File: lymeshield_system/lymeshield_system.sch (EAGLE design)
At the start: 67 parts, among them IC1 MCP79410-I_SN, J1 TSW-106-07-G-S, J2 M04B, J3 TSW-103-07-G-D-LL, J4 1844210, U1 ATMEGA1608-MU, U10 STSPIN240, U2 MX25V1635FM1I, U3 OPA2349EA, U4 DRV5057A2QDBZ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

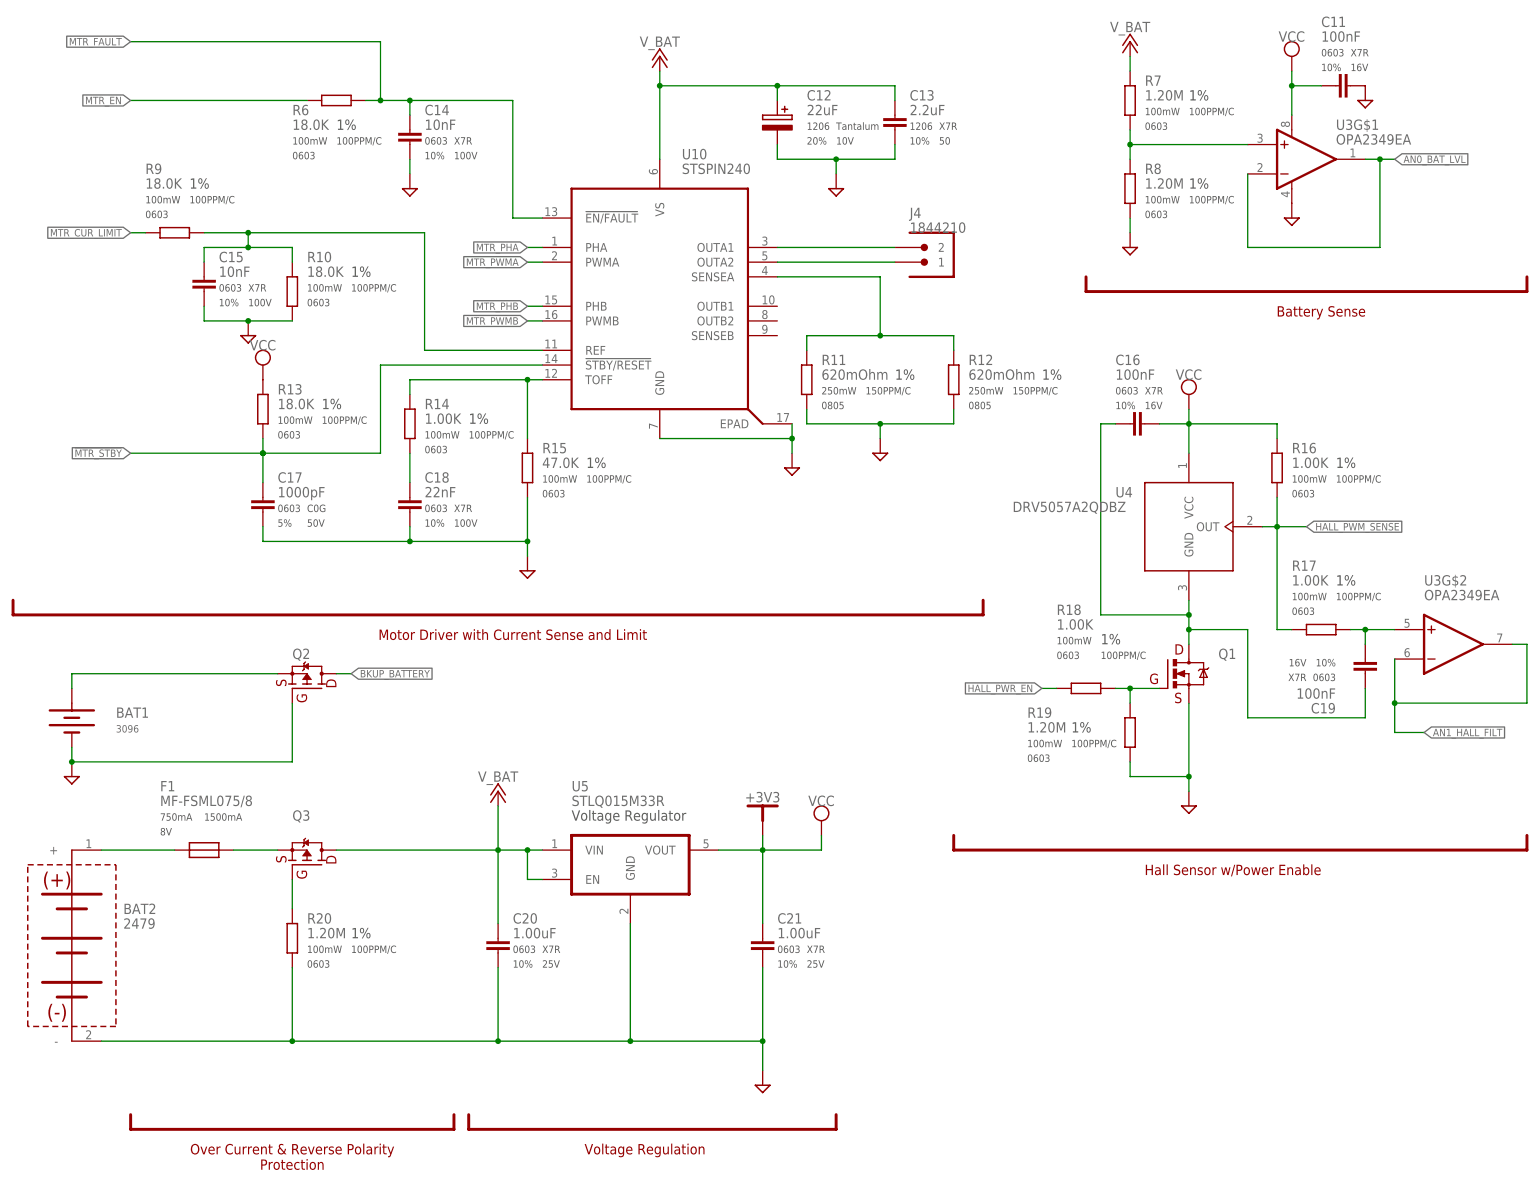
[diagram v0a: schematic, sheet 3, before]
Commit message: refactor: fixed ignored files and added tables
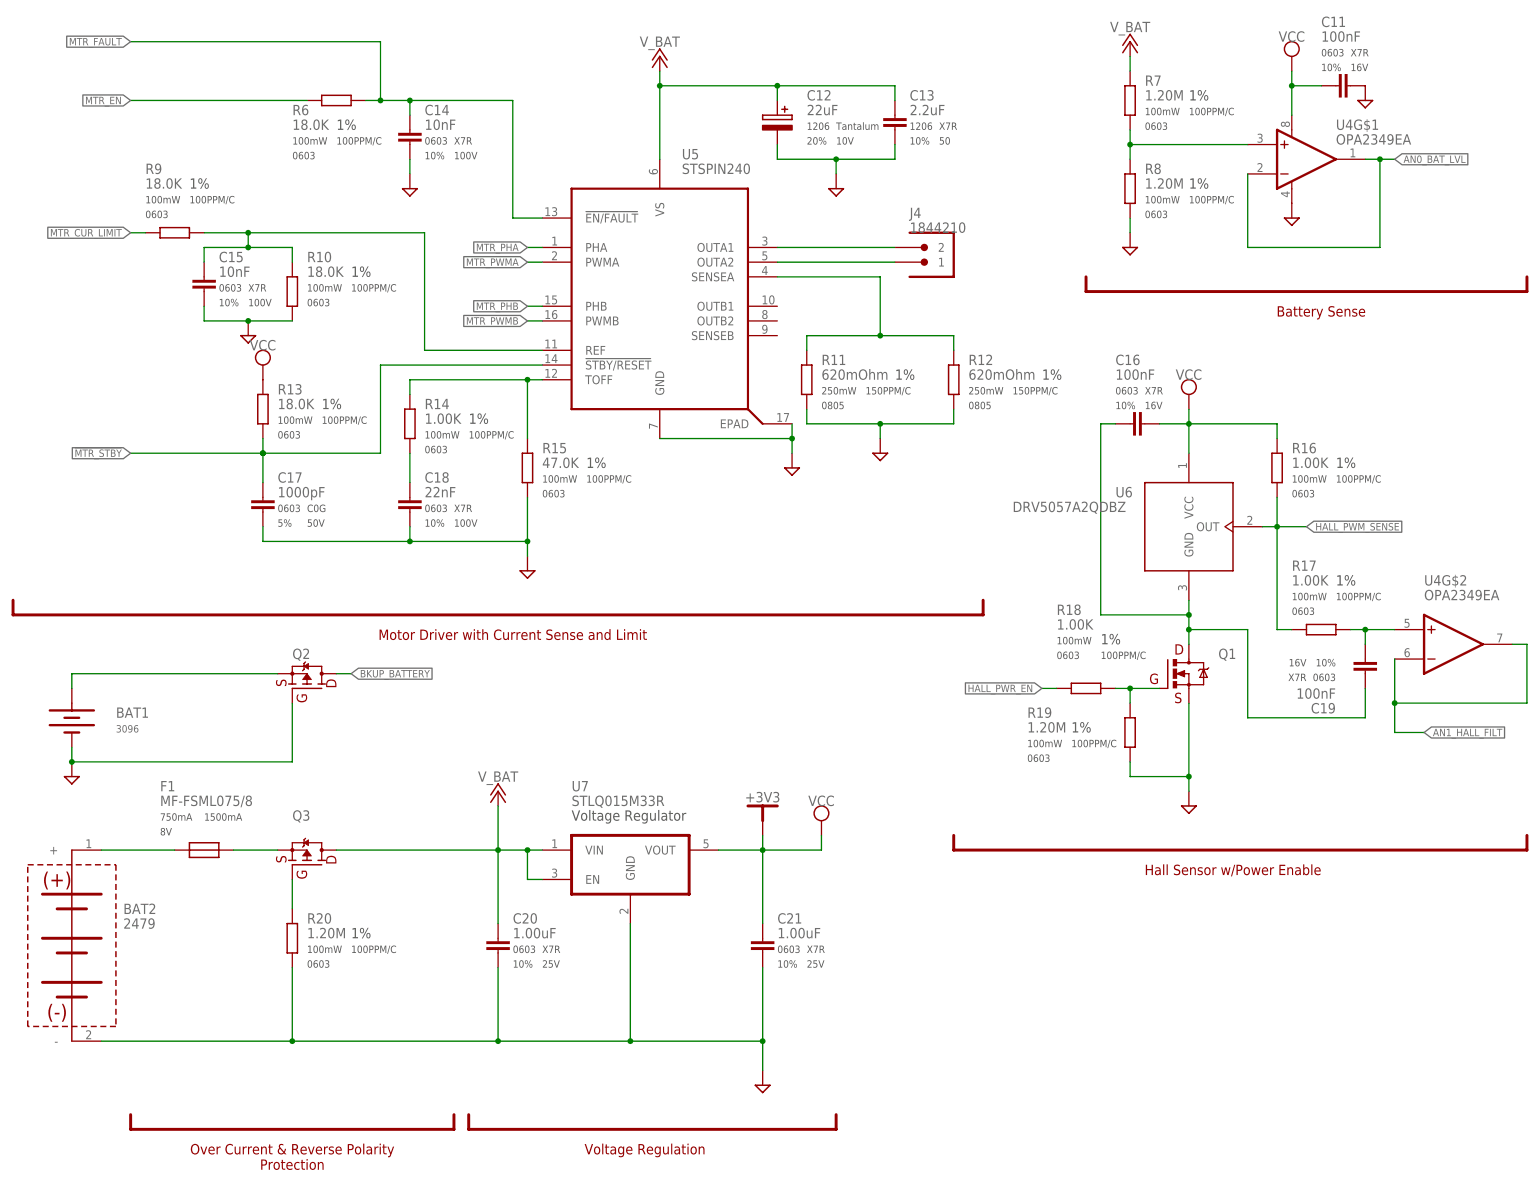
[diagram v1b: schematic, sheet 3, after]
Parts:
- removed IC1: MCP79410-I_SN, HatchPoint-MicrochipTechnology:MCP79410-I_SN
- removed U10: STSPIN240, HatchPoint-TI:STSPIN240
- added U6: DRV5057A2QDBZ, HatchPoint-TI:DRV5057A2QDBZ
- added U7: STLQ015M33R, HatchPoint-ST:STLQ015M33R
- U1: value ATMEGA1608-MU -> MCP79410-I_SN; device HatchPoint-MicrochipTechnology:ATMEGA1608-MU -> HatchPoint-MicrochipTechnology:MCP79410-I_SN
- U2: value MX25V1635FM1I -> ATMEGA1608-MU; device HatchPoint-Macronix:MX25V1635FM1I -> HatchPoint-MicrochipTechnology:ATMEGA1608-MU
- U3: value OPA2349EA -> MX25V1635FM1I; device HatchPoint-OPAMPs:OPA2349EA -> HatchPoint-Macronix:MX25V1635FM1I
- U4: value DRV5057A2QDBZ -> OPA2349EA; device HatchPoint-TI:DRV5057A2QDBZ -> HatchPoint-OPAMPs:OPA2349EA
- U5: value STLQ015M33R -> STSPIN240; device HatchPoint-ST:STLQ015M33R -> HatchPoint-TI:STSPIN240
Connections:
- net !CS_FLASH: now also U2.PA3, U3.!CS; no longer U1.PA3, U2.!CS
- net !GRN_LED_EN: now also U2.PD1; no longer U1.PD1
- net !MTR_FAULT: now also U2.PD5; no longer U1.PD5
- net !MTR_STBY: now also U2.PD7, U5.!STBY/RESET; no longer U1.PD7, U10.!STBY/RESET
- net !RED_LED_EN: now also U2.PD0; no longer U1.PD0
- net !RST: now also U2.PF6(!RST); no longer U1.PF6(!RST)
- net AN0_BAT_LVL: now also U2.PD3, U4G$1.-IN, U4G$1.OUT; no longer U1.PD3, U3G$1.-IN, U3G$1.OUT
- net AN1_HALL_FILT: now also U2.PD4, U4G$2.-IN, U4G$2.OUT; no longer U1.PD4, U3G$2.-IN, U3G$2.OUT
- net AVDD: now also U2.AVDD; no longer U1.AVDD
- net BKUP_BATTERY: now also U1.VBAT; no longer IC1.VBAT
- net DGND: now also U1.VSS, U2.EP, U2.GND@1, U2.GND@2, U3.GND, U4G$1.V-, U5.EPAD, U7.GND; no longer IC1.VSS, U1.EP, U1.GND@1, U1.GND@2, U10.EPAD, U10.GND, U2.GND, U3G$1.V-
- net GPIO_PC1: now also U2.PC1; no longer U1.PC1
- net HALL_PWM_SENSE: now also U2.PF4, U6.OUT; no longer U1.PF4, U4.OUT
- net HALL_PWR_EN: now also U2.PD6; no longer U1.PD6
- net I2C0_SCL: now also U1.SCL, U2.PC3; no longer IC1.SCL, U1.PC3
- net I2C0_SDA: now also U1.SDA, U2.PC2; no longer IC1.SDA, U1.PC2
- net MTR_CUR_LIMIT: now also U2.PD2; no longer U1.PD2
- net MTR_EN: now also U2.PF2; no longer U1.PF2
- net MTR_FAULT: now also U5.!EN/FAULT; no longer U10.!EN/FAULT
- net MTR_PHA: now also U2.PF3, U5.PHA; no longer U1.PF3, U10.PHA
- net MTR_PHB: now also U5.PHB; no longer U10.PHB
- net MTR_PWMA: now also U2.PF5, U5.PWMA; no longer U1.PF5, U10.PWMA
- net MTR_PWMB: now also U5.PWMB; no longer U10.PWMB
- net N$1: now also U2.PF0(TOSC1); no longer U1.PF0(TOSC1)
- net N$10: now also U4G$1.+IN; no longer U3G$1.+IN
- net N$16: now also U2.PF1(TOSC2); no longer U1.PF1(TOSC2)
- net N$17: now also U1.X1; no longer IC1.X1
- net N$19: now also U5.REF; no longer U10.REF
- net N$2: now also U1.X2; no longer IC1.X2
- net N$20: now also U4G$2.+IN; no longer U3G$2.+IN
- net N$23: now also U6.GND; no longer U4.GND
- net N$3: now also U5.TOFF; no longer U10.TOFF
- net OUTA1: now also U5.OUTA1; no longer U10.OUTA1
- net OUTA2: now also U5.OUTA2; no longer U10.OUTA2
- net RTCC_ALARM_INT: now also U1.MFP, U2.PA2; no longer IC1.MFP, U1.PA2
- net SENSEA: now also U5.SENSEA; no longer U10.SENSEA
- net SPI0_MISO: now also U2.PA5, U3.SO/SIO1; no longer U1.PA5, U2.SO/SIO1
- net SPI0_MOSI: now also U2.PA4, U3.SI/SIO0; no longer U1.PA4, U2.SI/SIO0
- net SPI0_SCK: now also U2.PA6, U3.SCLK; no longer U1.PA6, U2.SCLK
- net UART_RX: now also U2.PA1; no longer U1.PA1
- net UART_TX: now also U2.PA0(EXTCLK); no longer U1.PA0(EXTCLK)
- net UPDI: now also U2.UPDI; no longer U1.UPDI
- net VCC: now also U1.VCC, U2.VDD, U3.VCC, U4G$1.V+, U6.VCC, U7.VOUT; no longer IC1.VCC, U1.VDD, U2.VCC, U3G$1.V+, U4.VCC, U5.VOUT
- net V_BAT: now also U5.VS, U7.EN, U7.VIN; no longer U10.VS, U5.EN, U5.VIN
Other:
- note added: "12/02/2021"
- note added: "First document creation."
- note added: "R1,0"
- note added: "RSL"

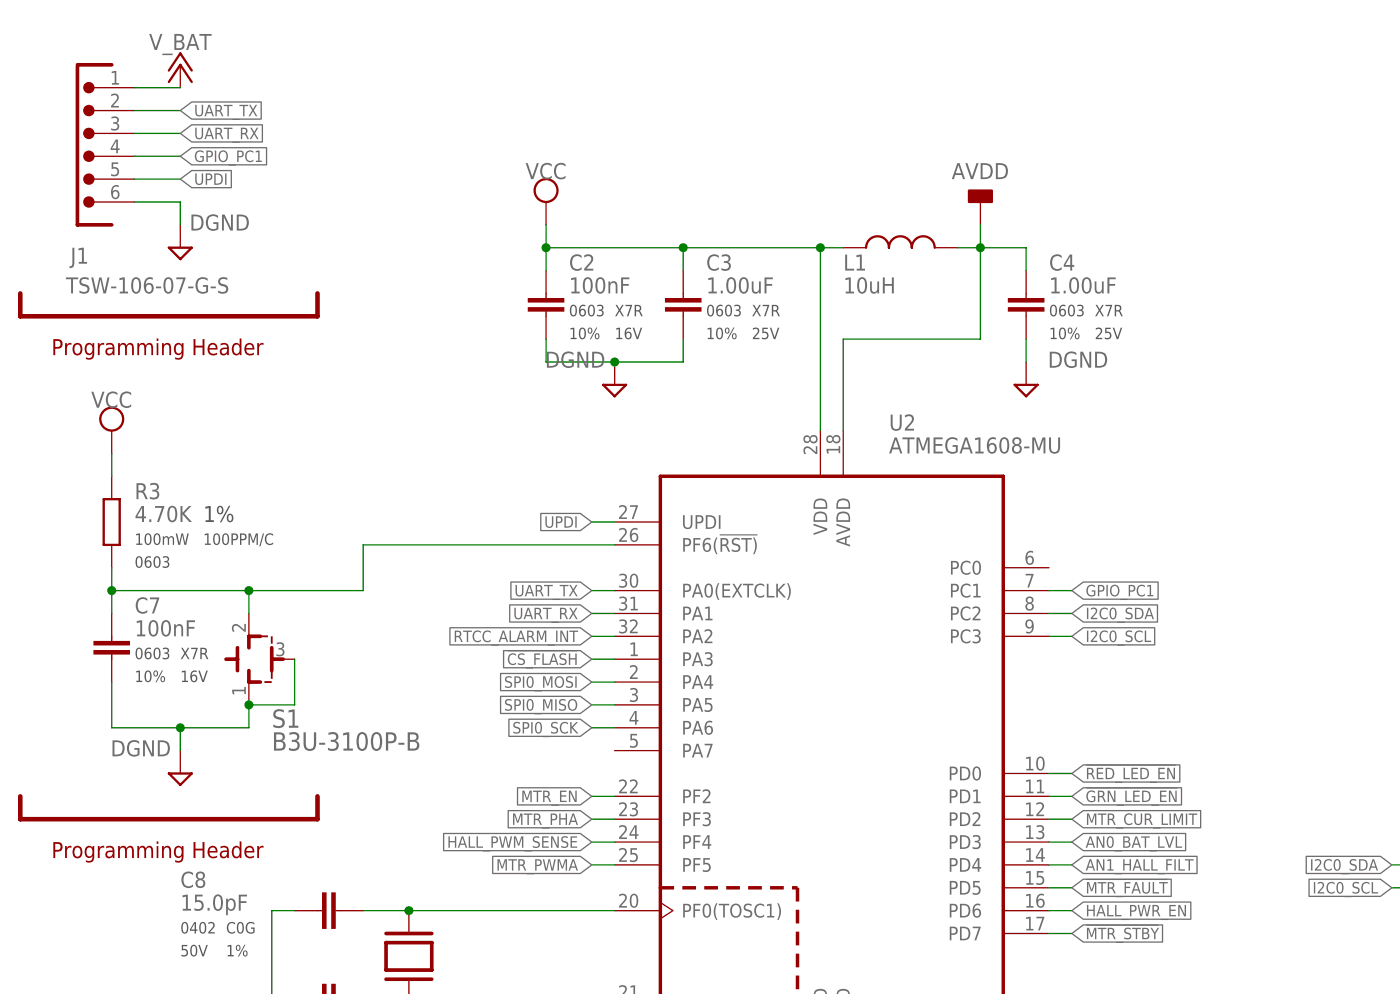
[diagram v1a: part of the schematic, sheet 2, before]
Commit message: feat: partial changes for r1,1 - Moved cur_limit to TBC0 pin - Modify layout to reduce EMI - Change programming header to match PICKit4 - Merge mtr_cur_limit into !mtr_cur_limit net
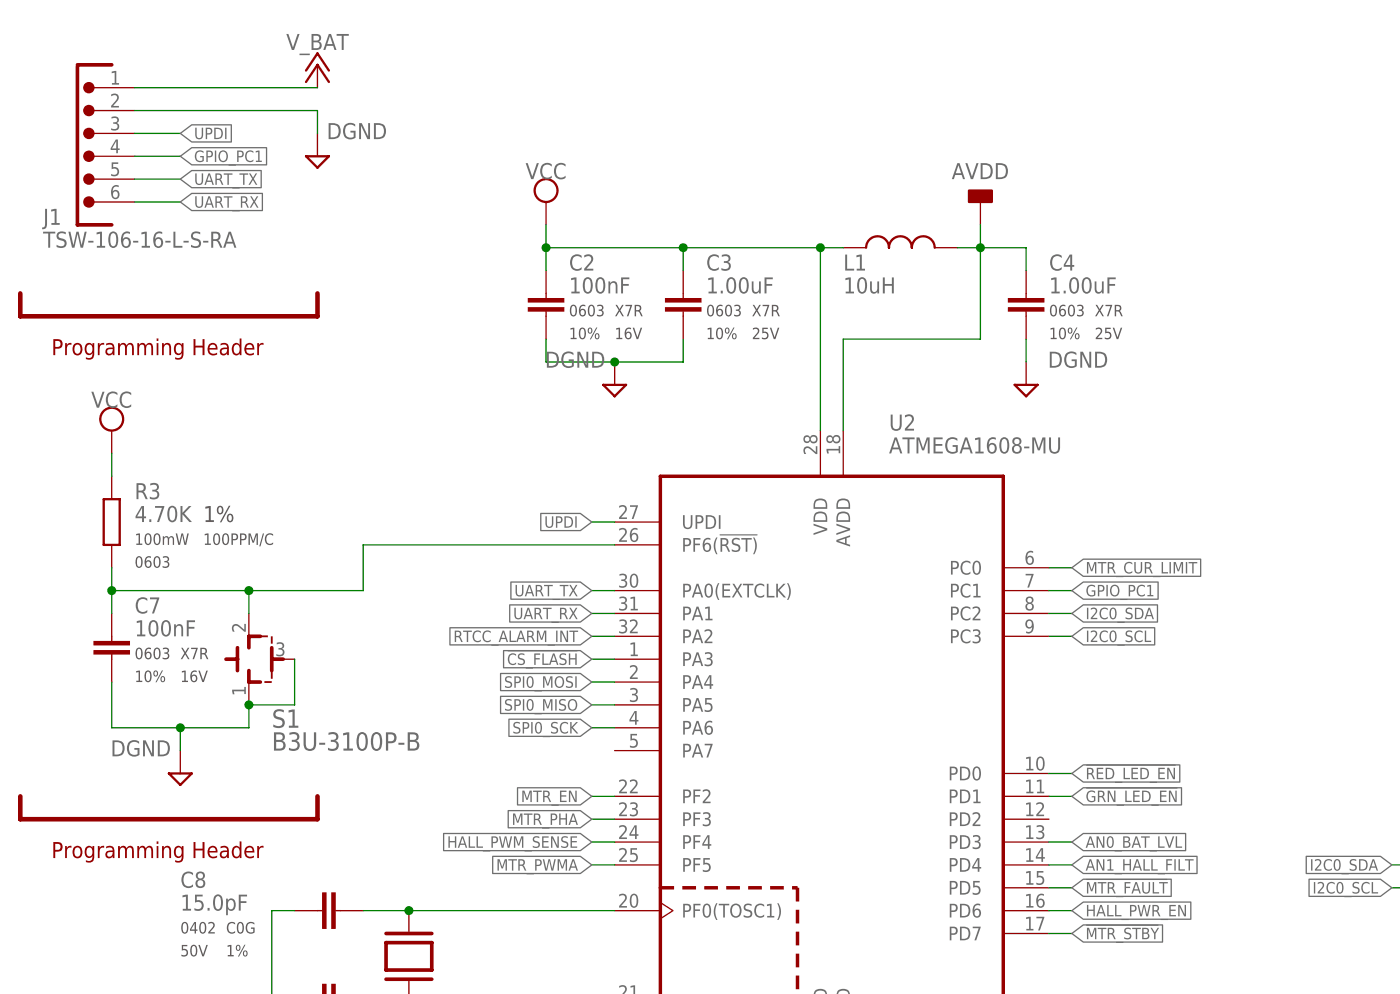
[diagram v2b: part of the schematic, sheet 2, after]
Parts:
- J1: value TSW-106-07-G-S -> TSW-106-16-L-S-RA; device HatchPoint-Samtec:TSW-106-07-G-S -> HatchPoint-Samtec:TSW-106-16-L-S-RA
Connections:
- removed net MTR_FAULT: C14.1, R6.2, U5.!EN/FAULT
- net !MTR_FAULT: now also C14.1, R6.2, U5.!EN/FAULT
- net DGND: now also J1.2; no longer J1.6
- net MTR_CUR_LIMIT: now also U2.PC0; no longer U2.PD2
- net UART_RX: now also J1.6; no longer J1.3
- net UART_TX: now also J1.5; no longer J1.2
- net UPDI: now also J1.3; no longer J1.5
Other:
- note added: "- Modify J1 pinout to match PICKit header - Correct MTR_FAULT net to !MTR_FAULT - Move MTR_CUR_LIMIT to TBC0 pin ()"
- note added: "02/08/2022"
- note added: "R1.0"
- note added: "R1.1"
- note removed: "R1,0"

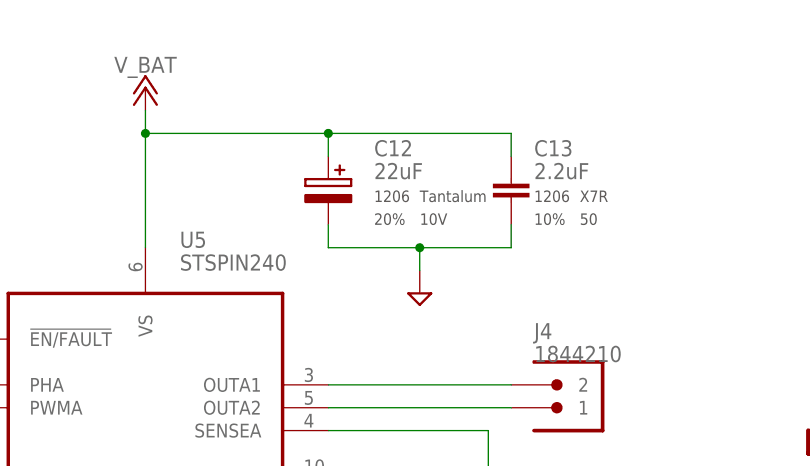
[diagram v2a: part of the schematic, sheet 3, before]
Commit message: fix: updates for R2.1 board - Change layout for high current routes - Correct routing errors (mtr_cur_limit) - Change tantalum cap to 1210 and give more space
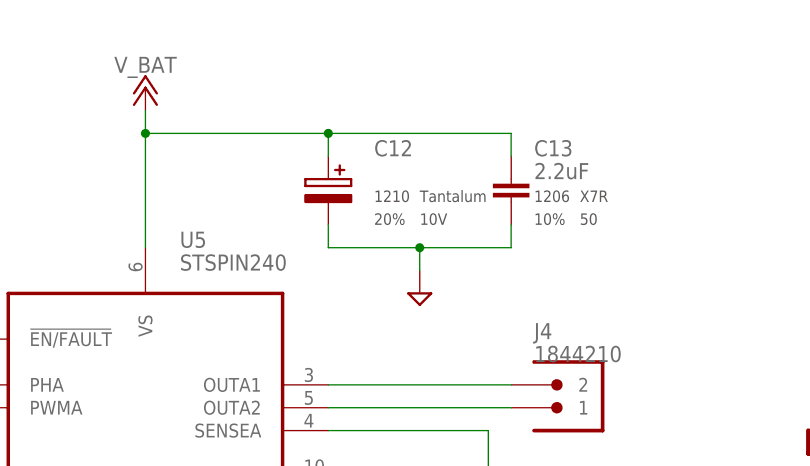
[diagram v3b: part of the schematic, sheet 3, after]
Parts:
- C12: value 22uF -> TAJB226M010RNJ; device HatchPoint-Capacitors:TAJC226M010RNJ -> HatchPoint-Capacitors:TAJB226M010RNJ; TYPE (none) -> Tantalum
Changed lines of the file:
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@@
 <part name="C17" library="HatchPoint-Capacitors" library_urn="urn:adsk.eagle:library:24125263" deviceset="GCM?*" device="188" package3d_urn="urn:adsk.eagle:package:24240850/4" technology="5C1H102JA16J" value="1000pF"/>
 <part name="C14" library="HatchPoint-Capacitors" library_urn="urn:adsk.eagle:library:24125263" deviceset="GCM?*" device="188" package3d_urn="urn:adsk.eagle:package:24240850/4" technology="R72A103KA37D" value="10nF"/>
-<part name="C12" library="HatchPoint-Capacitors" library_urn="urn:adsk.eagle:library:24125263" deviceset="TAJ?*" device="C" package3d_urn="urn:adsk.eagle:package:27805991/2" technology="226M010RNJ" value="22uF"/>
+<part name="C12" library="HatchPoint-Capacitors" library_urn="urn:adsk.eagle:library:24125263" deviceset="TAJ?*" device="B" package3d_urn="urn:adsk.eagle:package:34044660/2" technology="226M010RNJ" value="TAJB226M010RNJ">
+<attribute name="TYPE" value="Tantalum"/>
+</part>
 <part name="C21" library="HatchPoint-Capacitors" library_urn="urn:adsk.eagle:library:24125263" deviceset="GCM?*" device="188" package3d_urn="urn:adsk.eagle:package:24240850/4" technology="R71E105KA64D" value="1.00uF"/>
 <part name="C20" library="HatchPoint-Capacitors" library_urn="urn:adsk.eagle:library:24125263" deviceset="GCM?*" device="188" package3d_urn="urn:adsk.eagle:package:24240850/4" technology="R71E105KA64D" value="1.00uF"/>
@@
 <instance part="C12" gate="G$1" x="139.7" y="190.5" smashed="yes">
 <attribute name="NAME" x="144.78" y="190.5" size="1.778" layer="95"/>
-<attribute name="VALUE" x="144.78" y="187.96" size="1.778" layer="96"/>
 <attribute name="PACKAGE" x="144.78" y="185.42" size="1.27" layer="97"/>
 <attribute name="TOL" x="144.78" y="182.88" size="1.27" layer="97"/>
